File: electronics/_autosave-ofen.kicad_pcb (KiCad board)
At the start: 2 copper layers, 109.2 x 63.5 mm, 59 parts, among them IC1 TS4061BILT-1.225, IC2 MCP3461, J1 LEDs, J2 DB9_Female_MountingHoles, J3 12VDC, J4 CH0, J5 CH1, J6 UART, J7 ISP, J8 RST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

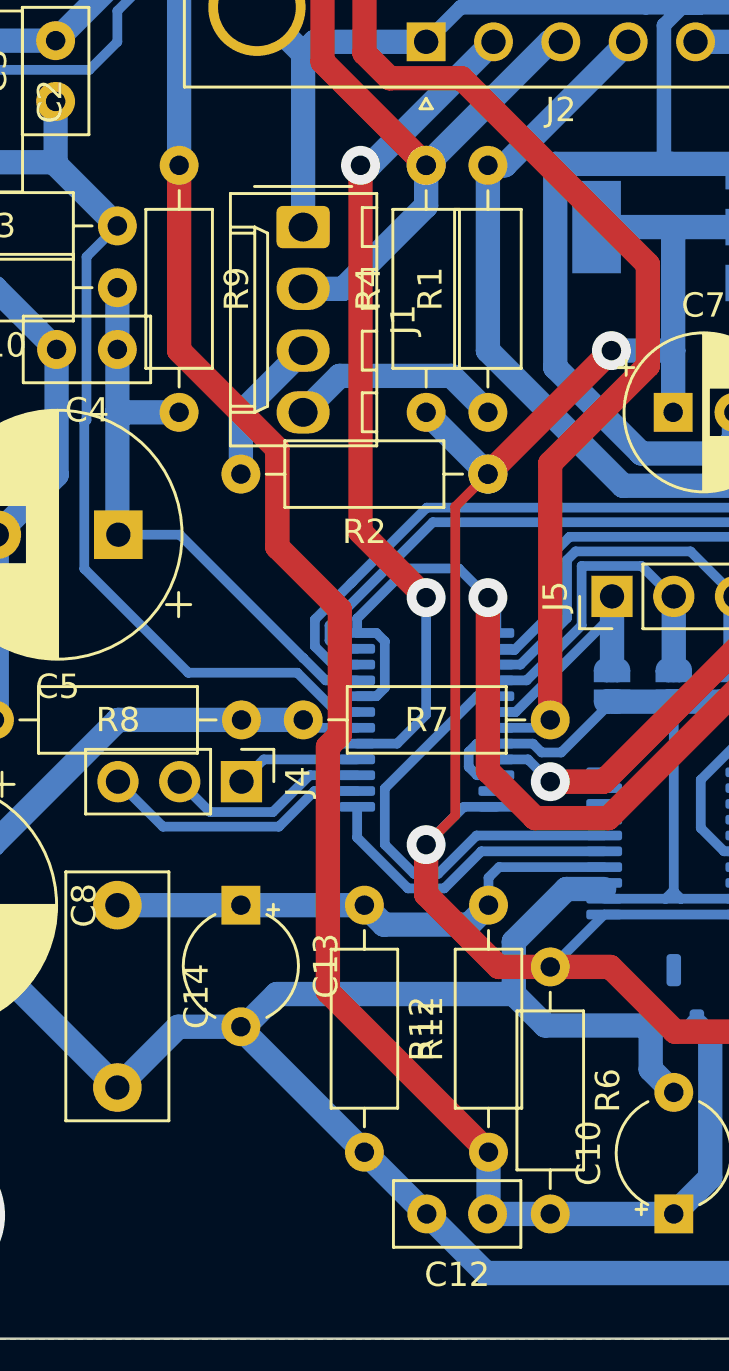
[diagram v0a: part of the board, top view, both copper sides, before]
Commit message: updated to version 2.1 of the pcb and added the first steps of the firmware
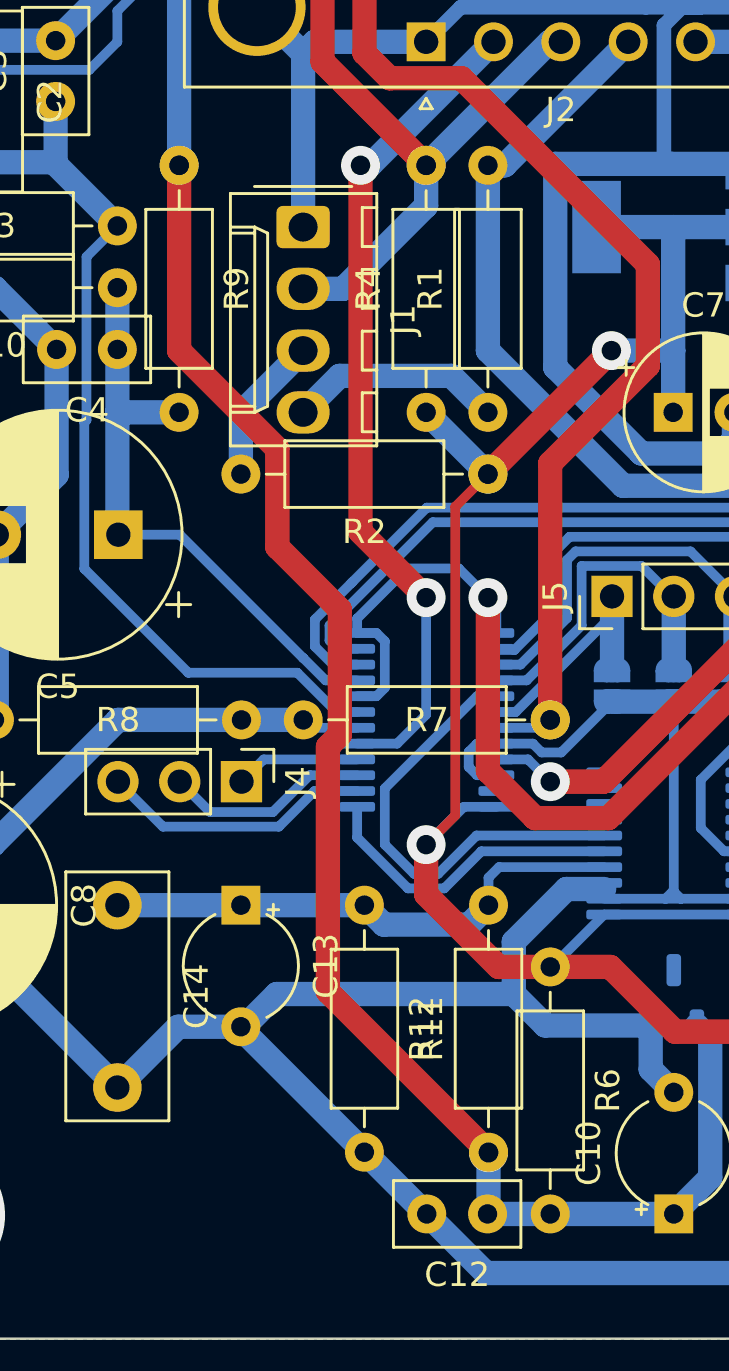
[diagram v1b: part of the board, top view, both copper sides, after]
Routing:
- net Net-(J2-Pad7): vias 1 -> 2
- net Net-(C10-Pad1): vias 0 -> 2
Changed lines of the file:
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@@
       (effects (font (size 1 1) (thickness 0.15)))
     )
-    (fp_text value "470" (at 2.54 2.54 90) (layer "F.Fab")
+    (fp_text value "470" (at 5.08 0 90) (layer "F.Fab")
       (effects (font (size 1 1) (thickness 0.15)))
     )
@@
       (effects (font (size 1 1) (thickness 0.15)))
     )
-    (fp_text value "3,3k" (at 2.54 2.54 90) (layer "F.Fab")
+    (fp_text value "3,3k" (at 5.08 0 90) (layer "F.Fab")
       (effects (font (size 1 1) (thickness 0.15)))
     )
@@
   (segment (start 146.28 103.1) (end 142.24 99.06) (width 1) (layer "F.Cu") (net 7))
   (segment (start 148.36 125.425) (end 148.36 115.356321) (width 1) (layer "F.Cu") (net 7))
+  (via (at 142.24 91.44) (size 1.6) (drill 0.8) (layers "F.Cu" "B.Cu") (net 7))
+  (via (at 154.965 132.055) (size 1.6) (drill 0.8) (layers "F.Cu" "B.Cu") (net 7))
   (segment (start 151.545 81.28) (end 144.78 81.28) (width 1) (layer "B.Cu") (net 7))
   (segment (start 157.505 134.57) (end 162.585 134.57) (width 1) (layer "B.Cu") (net 7))
@@
   (segment (start 164.085 133.07) (end 164.085 127.3675) (width 1) (layer "B.Cu") (net 7))
   (segment (start 142.24 83.82) (end 142.24 91.44) (width 1) (layer "B.Cu") (net 7))
-  (segment (start 154.965 132.03) (end 154.965 134.53) (width 1) (layer "B.Cu") (net 7))
+  (segment (start 154.965 132.03) (end 154.965 132.055) (width 1) (layer "B.Cu") (net 7))
   (segment (start 154.925 134.57) (end 157.505 134.57) (width 1) (layer "B.Cu") (net 7))
   (segment (start 153.785 83.52) (end 151.545 81.28) (width 1) (layer "B.Cu") (net 7))
   (segment (start 154.965 134.53) (end 154.925 134.57) (width 1) (layer "B.Cu") (net 7))
   (segment (start 162.585 134.57) (end 164.085 133.07) (width 1) (layer "B.Cu") (net 7))
+  (segment (start 154.965 132.055) (end 154.965 134.53) (width 1) (layer "B.Cu") (net 7))
   (segment (start 147.67 114.575) (end 147.345 114.25) (width 0.4) (layer "B.Cu") (net 8))
   (segment (start 144.805 114.25) (end 139.725 114.25) (width 1) (layer "B.Cu") (net 8))
@@
   (segment (start 149.86 84.038675) (end 152.4 81.498675) (width 1) (layer "F.Cu") (net 17))
   (segment (start 152.4 81.498675) (end 154.94 81.498675) (width 1) (layer "F.Cu") (net 17))
+  (via (at 157.505 114.25) (size 1.6) (drill 0.8) (layers "F.Cu" "B.Cu") (net 17))
   (via (at 154.94 81.498675) (size 1.6) (drill 0.8) (layers "F.Cu" "B.Cu") (net 17))
   (segment (start 155.2875 114.575) (end 157.18 114.575) (width 0.4) (layer "B.Cu") (net 17))
